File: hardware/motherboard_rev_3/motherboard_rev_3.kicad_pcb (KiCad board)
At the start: 2 copper layers, 82 x 54.8 mm, 67 parts, among them J1 Raspberry_Pi_2_3 ANT, J2 Conn_ST_STDC14, J3 Battery / Pitot/ Orientation, J4 c02 censor, J5 shaftencorder, J6 USB_C_Receptacle_USB2.0, J7 SparLoad, J8 lidar, J9 Control Board, Q1 2N7002K, SW1 MCU_RST, U10 TLV76733DRVx, U2 IMU, U3 LM358, U4 GPS module, U5 DHT11(DHT22), U6 STM32F412RETx, U7 nRF24L01-telemetry-INTERIOR, U8 nRF24L01-telemetry-EXTERIOR, U9 DPS310 - barometer, Y1 8M

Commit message: Settled on pin out
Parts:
- removed the C15 at (84.7, 82.6)
- removed the C16 at (95.0, 82.0)
- removed the C4 at (133.9, 100.1)
- removed C5: 100n, Capacitor_SMD:C_0603_1608Metric
- removed H1, H3, H4: MountingHole, MountingHole:MountingHole_2.5mm_Pad
- removed H5, H6, H7, H8: MountingHole, MountingHole:MountingHole_2.7mm_M2.5
- removed the J1 at (114.2, 70.2)
- removed the J3 at (76.0, 65.2)
- removed J7: SparLoad, Connector_JST:JST_EH_B3B-EH-A_1x03_P2.50mm_Vertical
- removed J8: lidar, Connector_JST:JST_EH_B4B-EH-A_1x04_P2.50mm_Vertical
- removed J9: Control Board, Connector_JST:JST_EH_B5B-EH-A_1x05_P2.50mm_Vertical
- removed JP4: 5V, Jumper:SolderJumper-2_P1.3mm_Open_RoundedPad1.0x1.5mm
- removed JP5, JP6: Jumper_2_Open, Jumper:SolderJumper-2_P1.3mm_Open_RoundedPad1.0x1.5mm
- removed Q1: 2N7002K, Package_TO_SOT_SMD:SOT-23
- removed R1: 100k, Resistor_SMD:R_0603_1608Metric
- removed the R15 at (84.7, 79.4)
- removed the R9 at (98.6, 82.0)
- removed the U3 at (90.3, 82.0)
- added BT1: XT30PW-M30.G.Y, Connector_AMASS:AMASS_XT30PW-M_1x02_P2.50mm_Horizontal, F.Cu at (77.4, 131.2)
- added C14: 100n, Capacitor_SMD:C_0402_1005Metric, F.Cu at (125.5, 148.1)
- added C18: 100n, Capacitor_SMD:C_0402_1005Metric, F.Cu at (125.5, 152.1)
- added C19: 1u, Capacitor_SMD:C_0603_1608Metric, F.Cu at (129.0, 148.3)
- added C2: 100n, Capacitor_SMD:C_0402_1005Metric, F.Cu at (122.7, 144.2)
- added C20: 10u, Capacitor_SMD:C_0603_1608Metric, F.Cu at (84.5, 118.3)
- added C21: 100n, Capacitor_SMD:C_0402_1005Metric, F.Cu at (84.0, 132.5)
- added C22: 100n, Capacitor_SMD:C_0402_1005Metric, F.Cu at (84.0, 130.6)
- added C23: 22u, Capacitor_SMD:C_0603_1608Metric, F.Cu at (84.5, 120.8)
- added C24: 100n, Capacitor_SMD:C_0402_1005Metric, F.Cu at (106.4, 146.9)
- added C25: 22u, Capacitor_SMD:C_0603_1608Metric, F.Cu at (84.5, 123.3)
- added C26: 10u, Capacitor_SMD:C_0603_1608Metric, F.Cu at (84.5, 125.8)
- added C27: 470n, Capacitor_SMD:C_0402_1005Metric, F.Cu at (84.0, 136.5)
- added C28: 470n, Capacitor_SMD:C_0402_1005Metric, F.Cu at (84.0, 140.4)
- added C29: 10u, Capacitor_SMD:C_0603_1608Metric, F.Cu at (84.5, 128.3)
- added C30: 1u, Capacitor_SMD:C_0402_1005Metric, F.Cu at (132.2, 139.6)
- added C31: 10u, Capacitor_SMD:C_0603_1608Metric, F.Cu at (137.8, 126.2)
- added C32: 10u, Capacitor_SMD:C_0603_1608Metric, F.Cu at (137.8, 128.7)
- added C33: 10u, Capacitor_SMD:C_0603_1608Metric, F.Cu at (137.8, 131.2)
- added C9: 100n, Capacitor_SMD:C_0402_1005Metric, F.Cu at (122.7, 152.1)
- added D4: SS34, Diode_SMD:D_SMA, F.Cu at (109.0, 135.6)
- added J5: Conn_01x04, Connector_JST:JST_EH_B4B-EH-A_1x04_P2.50mm_Vertical, F.Cu at (124.8, 127.5)
- added J6: Conn_01x04, Connector_JST:JST_EH_B4B-EH-A_1x04_P2.50mm_Vertical, F.Cu at (124.8, 133.4)
- added JP3: TERM, Jumper:SolderJumper-2_P1.3mm_Open_TrianglePad1.0x1.5mm, F.Cu at (128.6, 138.4)
- added L1: 3u3, Inductor_SMD:L_Changjiang_FNR6045S, F.Cu at (71.1, 137.7)
- added R11: 10k, Resistor_SMD:R_0603_1608Metric, F.Cu at (129.0, 150.8)
- added R18: 54k9, Resistor_SMD:R_0402_1005Metric, F.Cu at (88.0, 122.0)
- added R19: 10k, Resistor_SMD:R_0402_1005Metric, F.Cu at (88.0, 124.0)
- added R20: 120, Resistor_SMD:R_0402_1005Metric, F.Cu at (88.0, 120.0)
- added R21: 30k9, Resistor_SMD:R_0402_1005Metric, F.Cu at (88.0, 126.0)
- added R22: 10k, Resistor_SMD:R_0402_1005Metric, F.Cu at (88.0, 128.0)
- added R23: 120, Resistor_SMD:R_0402_1005Metric, F.Cu at (132.2, 137.6)
- added U11: INA219AIDCN, Package_TO_SOT_SMD:SOT-23-8, F.Cu at (88.0, 132.0)
- added U12: TPS7A8101, Package_SON:VSON-8-1EP_3x3mm_P0.65mm_EP1.65x2.4mm, F.Cu at (78.0, 136.3)
- added U13: TCAN3403, Package_TO_SOT_SMD:TSOT-23-8, F.Cu at (123.8, 139.0)
- added U4: BMP390, motherboard-footprints:LGA10_BMP390_BOS, F.Cu at (132.8, 148.9)
- C10: renamed from C2; value 4.7u -> 4u7
- C11, C12, C6, C7, C8: footprint Capacitor_SMD:C_0603_1608Metric -> Capacitor_SMD:C_0402_1005Metric
- C13, C17: value 0.22u -> 100n; footprint Capacitor_SMD:C_0603_1608Metric -> Capacitor_SMD:C_0402_1005Metric
- C3: value 2.2u -> 2u2
- JP1: value Jumper_3_Open -> SolderJumper_3_Open; footprint Jumper:SolderJumper-3_P2.0mm_Open_TrianglePad1.0x1.5mm_NumberLabels -> Jumper:SolderJumper-3_P1.3mm_Open_RoundedPad1.0x1.5mm
- R10: renamed from R12; value 130R -> 130
- R12: renamed from R5; value 22R -> 22
- R13: renamed from R6; value 22R -> 22
- R14: renamed from R7; value 5.1K -> 5k1
- R15: renamed from R8; value 5.1K -> 5k1
- R16: value 20k -> 120; footprint Resistor_SMD:R_0603_1608Metric -> Resistor_SMD:R_0402_1005Metric
- R17: value 470R -> 10m; footprint Resistor_SMD:R_0603_1608Metric -> Resistor_SMD:R_0805_2012Metric
- R4: renamed from R10; value 130R -> 130
- R5: renamed from R11; value 130R -> 130
- U10: value TLV76733DRVx -> TPS563201; footprint Package_SON:WSON-6-1EP_2x2mm_P0.65mm_EP1x1.6mm -> Package_TO_SOT_SMD:SOT-23-6
- U5: value DHT11(DHT22) -> BME280; footprint Sensor:Aosong_DHT11_5.5x12.0_P2.54mm -> Package_LGA:Bosch_LGA-8_2.5x2.5mm_P0.65mm_ClockwisePinNumbering
- U6: renamed from U8; value nRF24L01-telemetry-EXTERIOR -> nRF24L01
- U8: renamed from U7; value nRF24L01-telemetry-INTERIOR -> nRF24L01
- U9: value DPS310 - barometer -> BNO055; footprint Package_LGA:Bosch_LGA-8_2x2.5mm_P0.65mm_ClockwisePinNumbering -> Package_LGA:LGA-28_5.2x3.8mm_P0.5mm
- moved C7 70.0 mm to (122.7, 148.1), turned to 0 degrees
- moved U10 69.0 mm to (88.0, 136.6)
- moved C17 67.7 mm to (125.5, 150.1), turned to 0 degrees
- moved JP1 66.6 mm to (129.8, 145.0)
- moved C13 63.2 mm to (125.5, 146.2), turned to 0 degrees
- moved C6 59.1 mm to (122.7, 146.2), turned to 0 degrees
- moved R17 56.3 mm to (77.1, 140.0)
- moved C11 54.5 mm to (122.7, 154.0), turned to 0 degrees
- moved C8 53.6 mm to (122.7, 150.1), turned to 0 degrees
- moved U5 45.7 mm to (129.2, 154.3), turned to 0 degrees
- moved C12 44.7 mm to (125.5, 144.2), turned to 0 degrees
- moved U9 42.6 mm to (108.5, 140.7), turned to 0 degrees
- moved R16 37.1 mm to (88.0, 118.0)
- renumbered C9 to C15, C10 to C16, C1 to C4, J2 to J1, J6 to J2, J5 to J3, R3 to R6, R4 to R7, R13 to R8, R14 to R9, U4 to U1, U2 to U3, U6 to U7
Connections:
- C13 pad 1: Net-(JP5-A) -> +3.3V
- C17 pad 1: Net-(JP6-B) -> +3.3V
- C6 pad 1: GND -> +3.3V
- C6 pad 2: +3.3V -> GND
- C7 pad 1: GND -> +3.3V
- C7 pad 2: +3.3V -> GND
- C8 pad 1: GND -> +3.3V
- C8 pad 2: +3.3V -> GND
- J1 pad 12: unconnected-(J2-~{RST}-Pad12) -> /~{RST}
- J2 pad A4: +5V -> Net-(D4-A)
- J2 pad A9: +5V -> Net-(D4-A)
- J2 pad B4: +5V -> Net-(D4-A)
- J2 pad B9: +5V -> Net-(D4-A)
- J2 pad S1: unconnected-(J6-SHIELD-PadS1)_0 -> GND
- J3 pad 2: /SHAFTENC IN -> /ENC1
- J3 pad 3: /ENC1 -> /ENC2
- J3 pad 4: /ENC2 -> /ENC3
- J3 pad 5: /ENC3 -> /ENC4
- J3 pad 6: +5V -> Net-(J3-Pin_6)
- JP1 pad 1: /SHAFTENC IN -> +5V
- JP1 pad 2: /SHAFTENC OUT -> Net-(J3-Pin_6)
- JP1 pad 3: Net-(JP1-B) -> +3.3V
- R16 pad 1: +5V -> Net-(BT1-+)
- R17 pad 1: Net-(JP4-A) -> Net-(BT1-+)
- R17 pad 2: /SHAFTENC IN -> +BATT
- R7 pad 1: /RST -> /~{RST}
- SW1 pad 2: /RST -> /~{RST}
- U10 pad 1: Net-(JP5-A) -> GND
- U10 pad 2: Net-(JP5-A) -> Net-(U10-SW)
- U10 pad 3: GND -> +BATT
- U10 pad 4: Net-(JP6-B) -> Net-(U10-VFB)
- U10 pad 5: GND -> +BATT
- U10 pad 6: Net-(JP6-B) -> Net-(U10-VBST)
- U5 pad 1: +3.3V -> GND
- U5 pad 2: /DHT22 -> +3.3V
- U5 pad 3: unconnected-(U5-NC-Pad3) -> /I2C_{SDA}
- U5 pad 4: GND -> /I2C_{SCK}
- U7 pad 10: /OneWire_{RX} -> unconnected-(U7-PC2-Pad10)
- U7 pad 11: /OneWire_{TX} -> unconnected-(U7-PC3-Pad11)
- U7 pad 27: /DHT22 -> unconnected-(U7-PB1-Pad27)
- U7 pad 61: /SHAFTENC OUT -> unconnected-(U7-PB8-Pad61)
- U7 pad 7: /RST -> /~{RST}
- U9 pad 1: GND -> unconnected-(U9-PIN1-Pad1)
- U9 pad 2: unconnected-(U9-CSB-Pad2) -> GND
- U9 pad 3: /I2C_{SDA} -> +3.3V
- U9 pad 4: /I2C_{SCK} -> Net-(U9-~{BOOT_LOAD_PIN})
- U9 pad 5: unconnected-(U9-SDO-Pad5) -> GND
- U9 pad 6: +3.3V -> GND
- U9 pad 7: GND -> unconnected-(U9-PIN7-Pad7)
- U9 pad 8: +3.3V -> unconnected-(U9-PIN8-Pad8)
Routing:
- net /I2C_{SCK}: track 136.5 -> 48.0 mm
- net /I2C_{SDA}: track 141.9 -> 59.7 mm
- net /RST: track 72.3 -> 0.00 mm, vias 5 -> 0
- net /~{RST}: track 0.00 -> 71.5 mm, vias 0 -> 5
- net /OneWire_{RX}: track 42.5 -> 0.00 mm, vias 1 -> 0
- net +5V: track 216.5 -> 182.9 mm
- net /SHAFTENC IN: track 29.0 -> 0.00 mm, vias 2 -> 0
- net /ENC1: track 49.5 -> 78.5 mm, vias 2 -> 4
- net unconnected-(U7-PB8-Pad61): track 0.00 -> 27.3 mm, vias 0 -> 2
- net /SHAFTENC OUT: track 27.3 -> 0.00 mm, vias 2 -> 0
- net (no net): track 0.00 -> 26.3 mm, vias 0 -> 4
- net /DHT22: track 23.6 -> 0.00 mm, vias 1 -> 0
- net /USART3_{TX}: track 29.7 -> 11.6 mm
- net /USART3_{RX}: track 30.1 -> 15.3 mm
- net Net-(JP1-B): track 12.7 -> 0.00 mm, vias 2 -> 0
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
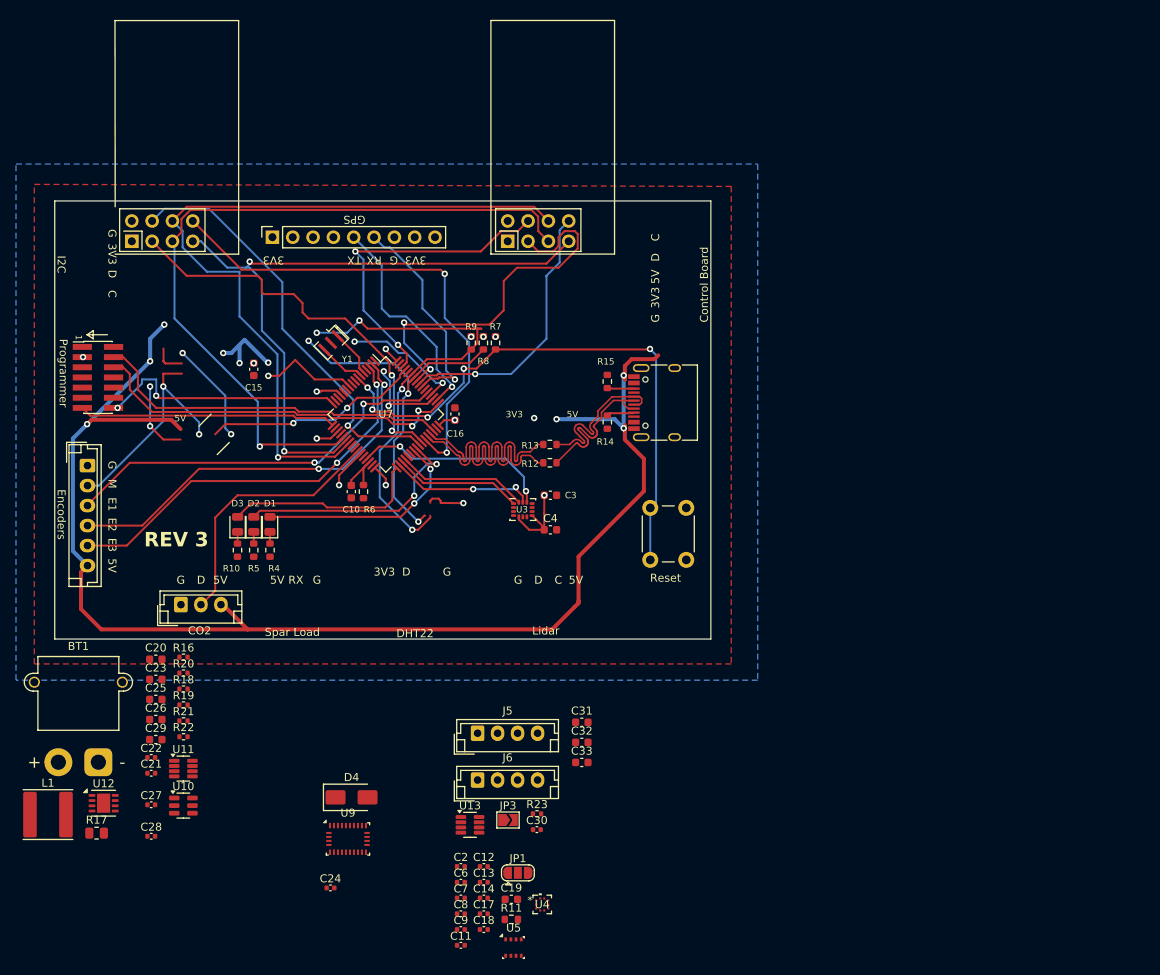
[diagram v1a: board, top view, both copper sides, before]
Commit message: Completed schematic for rev 3.0 PCB
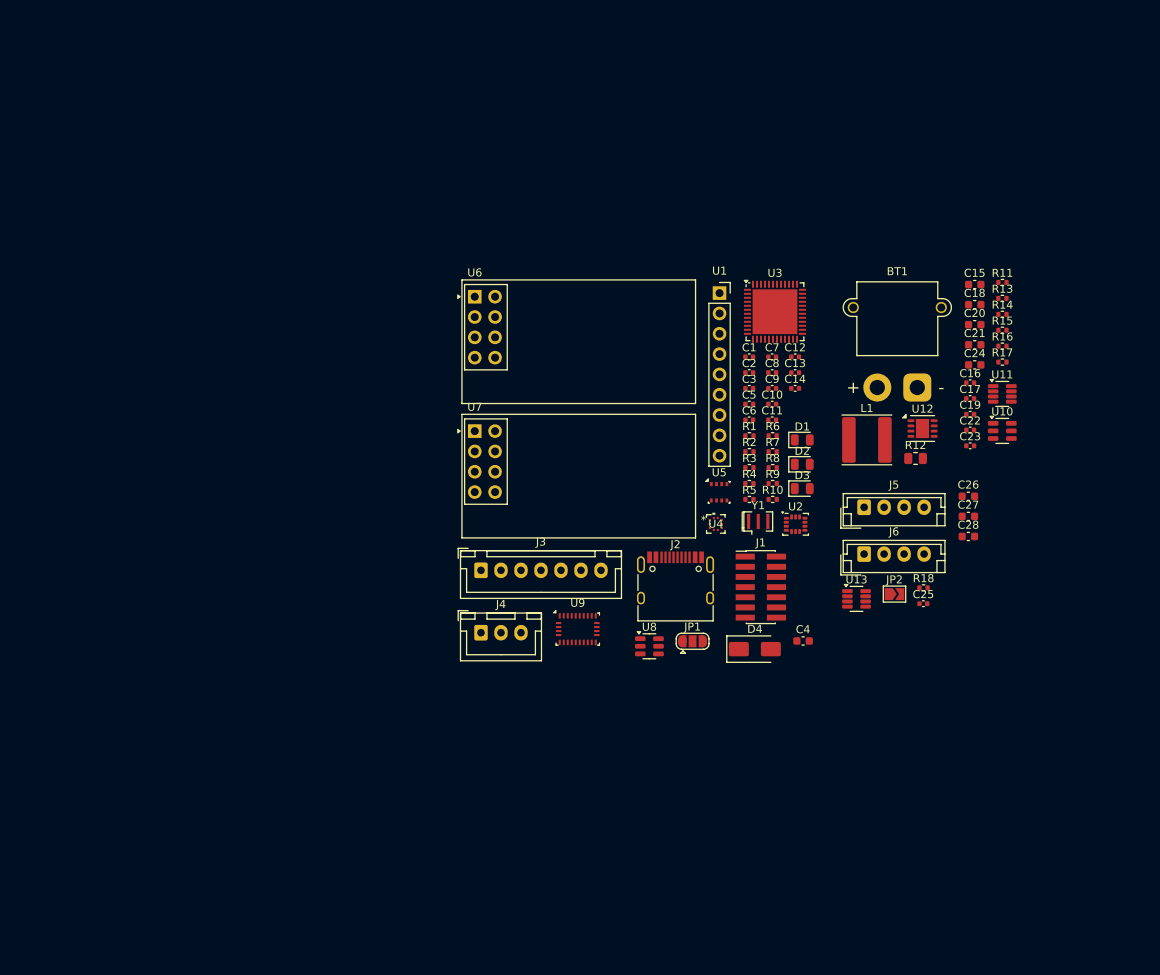
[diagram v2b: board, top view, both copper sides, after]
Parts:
- removed C29, C31, C32, C33: 10u, Capacitor_SMD:C_0603_1608Metric
- removed C30: 1u, Capacitor_SMD:C_0402_1005Metric
- removed JP3: TERM, Jumper:SolderJumper-2_P1.3mm_Open_TrianglePad1.0x1.5mm
- removed R19, R22: 10k, Resistor_SMD:R_0402_1005Metric
- removed R20, R23: 120, Resistor_SMD:R_0402_1005Metric
- removed R21: 30k9, Resistor_SMD:R_0402_1005Metric
- removed SW1: MCU_RST, Button_Switch_THT:SW_PUSH_6mm_H4.3mm
- added C1: 100n, Capacitor_SMD:C_0402_1005Metric, F.Cu at (158.7, 80.5)
- added C5: 100n, Capacitor_SMD:C_0402_1005Metric, F.Cu at (158.7, 86.4)
- added JP2: TERM, Jumper:SolderJumper-2_P1.3mm_Open_TrianglePad1.0x1.5mm, F.Cu at (176.9, 110.1)
- added R1: 5k1, Resistor_SMD:R_0402_1005Metric, F.Cu at (158.7, 90.3)
- added R2: 5k1, Resistor_SMD:R_0402_1005Metric, F.Cu at (158.7, 92.3)
- added R3: 10k, Resistor_SMD:R_0402_1005Metric, F.Cu at (158.7, 94.3)
- added U2: ICM-42688, Package_LGA:LGA-14_3x2.5mm_P0.5mm_LayoutBorder3x4y, F.Cu at (164.5, 101.4)
- C10: value 4u7 -> 100n; footprint Capacitor_SMD:C_0603_1608Metric -> Capacitor_SMD:C_0402_1005Metric
- C11, C14: value 100n -> 1u
- C15: value 10n -> 10u
- C16, C19: value 1u -> 100n; footprint Capacitor_SMD:C_0603_1608Metric -> Capacitor_SMD:C_0402_1005Metric
- C18: value 100n -> 22u; footprint Capacitor_SMD:C_0402_1005Metric -> Capacitor_SMD:C_0603_1608Metric
- C2: value 100n -> 2u2
- C20: value 10u -> 22u
- C21, C24: value 100n -> 10u; footprint Capacitor_SMD:C_0402_1005Metric -> Capacitor_SMD:C_0603_1608Metric
- C22: value 100n -> 470n
- C23: value 22u -> 470n; footprint Capacitor_SMD:C_0603_1608Metric -> Capacitor_SMD:C_0402_1005Metric
- C25: value 22u -> 1u; footprint Capacitor_SMD:C_0603_1608Metric -> Capacitor_SMD:C_0402_1005Metric
- C27, C28: value 470n -> 10u; footprint Capacitor_SMD:C_0402_1005Metric -> Capacitor_SMD:C_0603_1608Metric
- C3: value 2u2 -> 100n; footprint Capacitor_SMD:C_0603_1608Metric -> Capacitor_SMD:C_0402_1005Metric
- C4: value 10n -> 4u7
- D1: value LED -> RED
- D2: value LED -> WHITE
- D3: value LED -> GREEN
- J3: value shaftencorder -> Conn_01x07; footprint Connector_JST:JST_EH_B6B-EH-A_1x06_P2.50mm_Vertical -> Connector_JST:JST_XH_B7B-XH-A_1x07_P2.50mm_Vertical
- J4: value c02 censor -> Conn_01x03; footprint Connector_JST:JST_EH_B3B-EH-A_1x03_P2.50mm_Vertical -> Connector_JST:JST_XH_B3B-XH-A_1x03_P2.50mm_Vertical
- R10: value 130 -> 5k1; footprint Resistor_SMD:R_0603_1608Metric -> Resistor_SMD:R_0402_1005Metric
- R11, R7: value 10k -> 120; footprint Resistor_SMD:R_0603_1608Metric -> Resistor_SMD:R_0402_1005Metric
- R12: value 22 -> 10m; footprint Resistor_SMD:R_0603_1608Metric -> Resistor_SMD:R_0805_2012Metric
- R13: value 22 -> 54k9; footprint Resistor_SMD:R_0603_1608Metric -> Resistor_SMD:R_0402_1005Metric
- R14: value 5k1 -> 10k; footprint Resistor_SMD:R_0603_1608Metric -> Resistor_SMD:R_0402_1005Metric
- R15: value 5k1 -> 120; footprint Resistor_SMD:R_0603_1608Metric -> Resistor_SMD:R_0402_1005Metric
- R16: value 120 -> 30k9
- R17: value 10m -> 10k; footprint Resistor_SMD:R_0805_2012Metric -> Resistor_SMD:R_0402_1005Metric
- R18: value 54k9 -> 120
- R4: value 130 -> 100k; footprint Resistor_SMD:R_0603_1608Metric -> Resistor_SMD:R_0402_1005Metric
- R5: value 130 -> 120; footprint Resistor_SMD:R_0603_1608Metric -> Resistor_SMD:R_0402_1005Metric
- R6: value 100k -> 120; footprint Resistor_SMD:R_0603_1608Metric -> Resistor_SMD:R_0402_1005Metric
- R8: footprint Resistor_SMD:R_0603_1608Metric -> Resistor_SMD:R_0402_1005Metric
- R9: value 10k -> 5k1; footprint Resistor_SMD:R_0603_1608Metric -> Resistor_SMD:R_0402_1005Metric
- U3: value IMU -> STM32F412CGU6; footprint Package_LGA:LGA-14_3x2.5mm_P0.5mm_LayoutBorder3x4y -> Package_DFN_QFN:QFN-48-1EP_7x7mm_P0.5mm_EP5.6x5.6mm
- U7: value STM32F412RETx -> nRF24L01; footprint Package_QFP:LQFP-64_10x10mm_P0.5mm -> RF_Module:nRF24L01_Breakout
- U8: value nRF24L01 -> USBLC6-2SC6; footprint RF_Module:nRF24L01_Breakout -> Package_TO_SOT_SMD:SOT-23-6
- Y1: value 8M -> 20M
- moved R17 127.6 mm to (190.4, 81.1)
- moved C21 116.0 mm to (186.9, 79.0)
- moved U10 112.6 mm to (190.3, 89.7)
- moved U11 112.6 mm to (190.3, 85.1)
- moved U12 112.6 mm to (180.4, 89.4)
- moved BT1 112.6 mm to (179.7, 84.3)
- moved L1 112.6 mm to (173.4, 90.9)
- moved C20 110.6 mm to (186.9, 76.5)
- moved C22 110.2 mm to (186.3, 89.6)
- moved R16 109.5 mm to (190.4, 79.2)
- moved C28 108.8 mm to (186.1, 102.9)
- moved C27 108.3 mm to (186.1, 100.4)
- moved C23 105.9 mm to (186.3, 91.6)
- moved C26 105.3 mm to (186.1, 97.9)
- moved C24 103.7 mm to (186.9, 81.5)
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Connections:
- C10 pad 1: Net-(U7-VCAP_1) -> +3V3
- C11 pad 1: +3.3V -> GND
- C11 pad 2: GND -> +3V3
- C12 pad 1: +3.3V -> +3V3
- C13 pad 1: +3.3V -> +3V3
- C14 pad 1: +3.3V -> GND
- C14 pad 2: GND -> Net-(U9-CAP)
- C15 pad 1: GND -> +BATT
- C15 pad 2: +3.3V -> GND
- C16 pad 1: GND -> Net-(U10-VBST)
- C16 pad 2: +3.3V -> Net-(U10-SW)
- C17 pad 1: +3.3V -> Net-(U11-IN-)
- C17 pad 2: GND -> Net-(U11-IN+)
- C18 pad 1: +3.3V -> +5V
- C19 pad 1: GND -> +3V3
- C19 pad 2: Net-(U9-CAP) -> GND
- C2 pad 1: +3.3V -> +3V3
- C20 pad 1: +BATT -> +5V
- C21 pad 1: Net-(U10-VBST) -> +5V
- C21 pad 2: Net-(U10-SW) -> GND
- C22 pad 1: Net-(U11-IN-) -> Net-(U12-NR)
- C22 pad 2: Net-(U11-IN+) -> GND
- C23 pad 1: +5V -> +3V3
- C23 pad 2: GND -> Net-(U12-FB)
- C25 pad 1: +5V -> +3V3
- C26 pad 1: +5V -> +BATT
- C27 pad 1: Net-(U12-NR) -> +BATT
- C28 pad 1: +3V3 -> +BATT
- C28 pad 2: Net-(U12-FB) -> GND
- C3 pad 1: +3.3V -> +3V3
- C4 pad 1: +3.3V -> Net-(U3-VCAP_1)
- C6 pad 1: +3.3V -> +3V3
- C7 pad 1: +3.3V -> +3V3
- C8 pad 1: +3.3V -> +3V3
- C9 pad 1: +3.3V -> +3V3
- D1 pad 2: /LED1 -> /LED_ERROR
- D2 pad 2: /LED2 -> /LED_IND
- D3 pad 2: /LED3 -> /LED_HRTBT
- J1 pad 13: /USART2_{RX} -> /DEBUG_RX
- J1 pad 14: /USART2_{TX} -> /DEBUG_TX
- J1 pad 3: +3.3V -> +3V3
- J2 pad A6: /D+ -> /PORT-
- J2 pad A7: /D- -> /PORT+
- J2 pad B6: /D+ -> /PORT-
- J2 pad B7: /D- -> /PORT+
- J3 pad 6: Net-(J3-Pin_6) -> /ENC5
- JP1 pad 2: Net-(J3-Pin_6) -> Net-(J3-Pin_7)
- JP1 pad 3: +3.3V -> +3V3
- R10 pad 1: Net-(D3-K) -> GND
- R10 pad 2: GND -> Net-(J2-CC2)
- R11 pad 1: +3.3V -> Net-(BT1-+)
- R11 pad 2: Net-(U9-~{BOOT_LOAD_PIN}) -> Net-(U11-IN+)
- R12 pad 1: /USB- -> Net-(BT1-+)
- R12 pad 2: /D- -> +BATT
- R13 pad 1: /USB+ -> +5V
- R13 pad 2: /D+ -> Net-(U10-VFB)
- R14 pad 1: GND -> Net-(U10-VFB)
- R14 pad 2: Net-(J2-CC1) -> GND
- R15 pad 1: GND -> +BATT
- R15 pad 2: Net-(J2-CC2) -> Net-(U11-IN-)
- R16 pad 1: Net-(BT1-+) -> +3V3
- R16 pad 2: Net-(U11-IN+) -> Net-(U12-FB)
- R17 pad 1: Net-(BT1-+) -> Net-(U12-FB)
- R17 pad 2: +BATT -> GND
- R18 pad 1: +5V -> /CAN/CANH
- R18 pad 2: Net-(U10-VFB) -> Net-(JP2-A)
- R4 pad 2: Net-(D1-K) -> Net-(U3-VCAP_1)
- R5 pad 2: Net-(D2-K) -> Net-(D1-K)
- R6 pad 2: Net-(U7-VCAP_1) -> Net-(D2-K)
- R7 pad 1: /~{RST} -> Net-(D3-K)
- R7 pad 2: +3.3V -> GND
- R8 pad 1: +3.3V -> +3V3
- R8 pad 2: /I2C_{SCK} -> Net-(U9-~{BOOT_LOAD_PIN})
- R9 pad 1: +3.3V -> GND
- R9 pad 2: /I2C_{SDA} -> Net-(J2-CC1)
- U1 pad 1: +3.3V -> +3V3
- U1 pad 5: /USART1_{TX} -> /GPS_TX
- U1 pad 6: /USART1_{RX} -> /GPS_RX
- U1 pad 8: +3.3V -> +3V3
- U11 pad 5: /I2C_{SCK} -> /SCL
- U11 pad 6: /I2C_{SDA} -> /SDA
- U13 pad 1: /CAN/CAN_TX -> /CAN_TX
- U13 pad 4: /CAN/CAN_RX -> /CAN_RX
- U3 pad 1: /SPI2MISO -> unconnected-(U3-VBAT-Pad1)
- U3 pad 10: GND -> /CO_{2}
- U3 pad 11: GND -> /RADIO_EXT_CE
- U3 pad 12: /IMU_{CS} -> /GPS_RX
- U3 pad 13: /SPI2SCK -> /GPS_TX
- U3 pad 14: /SPI2MOSI -> /RADIO_EXT_CS
- U3 pad 2: GND -> /RADIO_INT_CE
- U3 pad 3: GND -> /RADIO_INT_IRQ
- U3 pad 4: unconnected-(U3-INT1-Pad4) -> /RADIO_EXT_IRQ
- U3 pad 5: +3.3V -> /XTAL_1
- U3 pad 6: GND -> /XTAL_2
- U3 pad 7: GND -> /~{RST}
- U3 pad 8: +3.3V -> GND
- U3 pad 9: unconnected-(U3-INT2-Pad9) -> +3V3
- U4 pad 1: +3.3V -> +3V3
- U4 pad 10: +3.3V -> +3V3
- U4 pad 2: /I2C_{SCK} -> /SCL
- U4 pad 4: /I2C_{SDA} -> /SDA
- U4 pad 6: +3.3V -> +3V3
- U5 pad 2: +3.3V -> +3V3
- U5 pad 3: /I2C_{SDA} -> /SDA
- U5 pad 4: /I2C_{SCK} -> /SCL
- U5 pad 5: +3.3V -> +3V3
- U5 pad 6: +3.3V -> +3V3
- U5 pad 8: +3.3V -> +3V3
- U6 pad 2: +3.3V -> +3V3
- U6 pad 3: /TELE_{CE}-E -> /RADIO_EXT_CE
- U6 pad 4: /TELE_{CS}-E -> /RADIO_EXT_CS
- U6 pad 5: /SPI1SCK -> /RADIO_{SCK}
- U6 pad 6: /SPI1MOSI -> /RADIO_{MOSI}
- U6 pad 7: /SPI1MISO -> /RADIO_{MISO}
- U6 pad 8: /TELE_{IRQ}-E -> /RADIO_EXT_IRQ
- U7 pad 1: unconnected-(U7-VBAT-Pad1) -> GND
- U7 pad 2: /ENC2 -> +3V3
- U7 pad 3: /ENC3 -> /RADIO_INT_CE
- U7 pad 4: unconnected-(U7-PC15-Pad4) -> /RADIO_INT_CS
- U7 pad 5: Net-(U7-PH0) -> /RADIO_{SCK}
- U7 pad 6: Net-(U7-PH1) -> /RADIO_{MOSI}
- U7 pad 7: /~{RST} -> /RADIO_{MISO}
- U7 pad 8: unconnected-(U7-PC0-Pad8) -> /RADIO_INT_IRQ
- U8 pad 1: GND -> /PORT+
- U8 pad 2: +3.3V -> GND
- U8 pad 3: /TELE_{CE}-int -> /PORT-
- U8 pad 4: /TELE_{CS}-int -> /USB+
- U8 pad 5: /SPI1SCK -> Net-(D4-A)
- U8 pad 6: /SPI1MOSI -> /USB-
- U9 pad 11: +3.3V -> +3V3
- U9 pad 19: /I2C_{SCK} -> /SCL
- U9 pad 20: /I2C_{SDA} -> /SDA
- U9 pad 28: +3.3V -> +3V3
- U9 pad 3: +3.3V -> +3V3
- Y1 pad 1: Net-(U7-PH0) -> /XTAL_1
- Y1 pad 3: Net-(U7-PH1) -> /XTAL_2
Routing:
- net +5V: track 182.9 -> 0.00 mm, vias 9 -> 0
- net /SPI1MOSI: track 95.6 -> 0.00 mm, vias 1 -> 0
- net /SPI1SCK: track 93.5 -> 0.00 mm, vias 1 -> 0
- net /SPI1MISO: track 83.9 -> 0.00 mm, vias 2 -> 0
- net /ENC1: track 78.5 -> 0.00 mm, vias 4 -> 0
- net /~{RST}: track 71.5 -> 0.00 mm, vias 5 -> 0
- net /TELE_{IRQ}-E: track 62.4 -> 0.00 mm, vias 2 -> 0
- net /I2C_{SDA}: track 59.7 -> 0.00 mm, vias 4 -> 0
- net /TELE_{CS}-E: track 52.6 -> 0.00 mm, vias 1 -> 0
- net /ENC2: track 50.8 -> 0.00 mm, vias 2 -> 0
- net /TELE_{CE}-E: track 50.8 -> 0.00 mm, vias 2 -> 0
- net /ENC3: track 50.0 -> 0.00 mm, vias 2 -> 0
- net /I2C_{SCK}: track 48.0 -> 0.00 mm, vias 3 -> 0
- net /TELE_{CE}-int: track 47.9 -> 0.00 mm, vias 2 -> 0
- net /SWCLK: track 46.9 -> 0.00 mm, vias 2 -> 0
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- removed copper zone on B.Cu, net +3.3V
- removed copper zone on F.Cu, net GND
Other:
- board outline removed
- board text removed: "1"
- board text removed: "3V3"
- board text removed: "5V"
- board text removed: "C"
- board text removed: "CO2"
- board text removed: "Control Board"
- board text removed: "D"
- board text removed: "DHT22"
- board text removed: "E1"
- board text removed: "E2"
- board text removed: "E3"
- board text removed: "Encoders"
- board text removed: "Ethan Todd"
- board text removed: "Falcon Motherboard"
- board text removed: "G"
- board text removed: "GPS"
- board text removed: "Human Powered Vehicles Design Team"
- board text removed: "I2C"
- board text removed: "Lidar"
- board text removed: "M"
- board text removed: "Programmer"
- board text removed: "REV 3"
- board text removed: "RX"
- board text removed: "Reset"
- board text removed: "Spar Load"
- board text removed: "TX"
- board text removed: "University of Toronto"
